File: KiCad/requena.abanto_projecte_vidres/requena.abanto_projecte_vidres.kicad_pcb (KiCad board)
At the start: 4 copper layers, 107.8 x 82.4 mm, 90 parts, among them J1 Conn_01x05, J3 DE9_Pins, J4 DE9_Pins, J5 Conn_01x02, P1 282837-2, P2 282837-2, SW1 SW_Push_SPDT, SW2 SW_Push, SW3 SW_Omron_B3FS, SW4 SW_Omron_B3FS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

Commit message: --
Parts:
- moved R1 9.97 mm to (120.8, 45.9), turned to -90 degrees
- moved R3 9.38 mm to (109.6, 45.6), turned to 90 degrees
- moved R2 8.79 mm to (106.7, 45.6)
- moved C6 6.51 mm to (114.2, 51.8), turned to 180 degrees
- moved U3 3.76 mm to (114.3, 45.2), turned to -90 degrees
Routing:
- net SCK: track 38.5 -> 4.40 mm
- net SHUNT: track 26.8 -> 0.00 mm
- net CAN_RX: track 40.3 -> 61.8 mm
- net AN0: track 55.9 -> 41.0 mm, vias 2 -> 1
- net GND: track 98.7 -> 85.1 mm, vias 94 -> 85
- net IRQ: track 37.4 -> 25.1 mm
- net REALIMENTACION_NOINV: track 12.2 -> 0.00 mm
- net OUTJUMPER: track 24.7 -> 13.4 mm
- net OUTSHUNT: track 9.67 -> 0.00 mm
- net OUTNOINV: track 8.93 -> 0.00 mm
- net VCC: track 50.3 -> 45.0 mm, vias 55 -> 52
- net SDA: track 43.1 -> 46.0 mm
- net CAN_TX: track 39.6 -> 37.3 mm
- net MCLR: track 17.2 -> 18.1 mm
- net MISO: track 35.0 -> 35.5 mm

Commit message: joan canals el mejor
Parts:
- C34, C35, C36, C37: moved to B.Cu
- moved FB1 96.7 mm to (86.9, 125.0)
- moved SW4 55.6 mm to (131.3, 106.0), turned to 90 degrees
- moved R8 47.9 mm to (131.9, 98.4), turned to 180 degrees
- moved J4 43.0 mm to (154.2, 100.5), turned to 0 degrees
- moved R9 38.3 mm to (131.7, 67.2), turned to 180 degrees
- moved SW3 34.6 mm to (140.6, 90.3), turned to 90 degrees
- moved J3 32.6 mm to (186.6, 100.5), turned to 0 degrees
- moved SW5 31.9 mm to (131.3, 74.7), turned to 90 degrees
- moved R7 31.6 mm to (141.2, 82.8), turned to 180 degrees
- moved R11 29.9 mm to (160.5, 96.8), turned to 180 degrees
- moved SW6 28.2 mm to (131.2, 90.3), turned to 90 degrees
- moved R10 27.5 mm to (131.7, 82.6), turned to 180 degrees
- moved SW2 24.1 mm to (140.5, 105.7), turned to -90 degrees
- moved U5 23.5 mm to (160.5, 91.3), turned to -90 degrees
- moved C34 21.8 mm to (194.4, 83.9)
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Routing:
- net CAN_RX: track 61.8 -> 6.03 mm, vias 2 -> 0
- net UP_W: track 67.3 -> 20.8 mm
- net DOWN_W: track 78.3 -> 36.8 mm, vias 0 -> 2
- net AN0: track 41.0 -> 1.53 mm
- net OUTJUMPER: track 13.4 -> 45.7 mm, vias 0 -> 2
- net SCK: track 4.40 -> 36.5 mm
- net CAN_TX: track 37.3 -> 6.11 mm
- net CLOSE_D: track 56.0 -> 32.5 mm
- net OPEN_D: track 44.9 -> 29.6 mm
- net PWM: track 31.3 -> 16.5 mm
- net UART_RX: track 54.3 -> 41.2 mm
- net IRQ: track 25.1 -> 37.4 mm
- net CLOSED_FC: track 12.0 -> 23.4 mm
- net INA: track 27.8 -> 39.0 mm
- net INB: track 34.0 -> 44.2 mm
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
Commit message: algunes millores
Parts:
- added TP1: TestPoint, TestPoint:TestPoint_Pad_1.5x1.5mm, F.Cu at (181.8, 86.1)
- added TP3: TestPoint, TestPoint:TestPoint_Pad_1.5x1.5mm, B.Cu at (193.6, 97.3)
- added TP4: TestPoint, TestPoint:TestPoint_Pad_1.5x1.5mm, B.Cu at (181.9, 99.9)
- added TP5: TestPoint, TestPoint:TestPoint_Pad_1.5x1.5mm, B.Cu at (136.0, 58.5)
- C20, C26: value C_Small -> 150 pF
- C27, C28: value C_Small -> 22 pF
- C29, C30: value C_Small -> 47 pF
- C31: value C_Small -> 1nF
- C32: value C_Small -> 100nF
- L1, L2: value L -> 2.2 uH
- L3: value L -> 1.5 uH
- R15, R16: value R -> 1.5
- R17: value R -> 2,2 k
- R18: value R -> 1k
- moved FB1 26.1 mm to (112.8, 121.9)
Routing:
- net AN0: track 1.53 -> 65.7 mm, vias 1 -> 2
- net PWM: track 16.5 -> 43.1 mm
- net VCC: track 53.8 -> 59.0 mm
- net UART_RX: track 41.2 -> 45.9 mm
- net UART_TX: track 44.6 -> 48.6 mm
- net GND: track 79.2 -> 82.1 mm

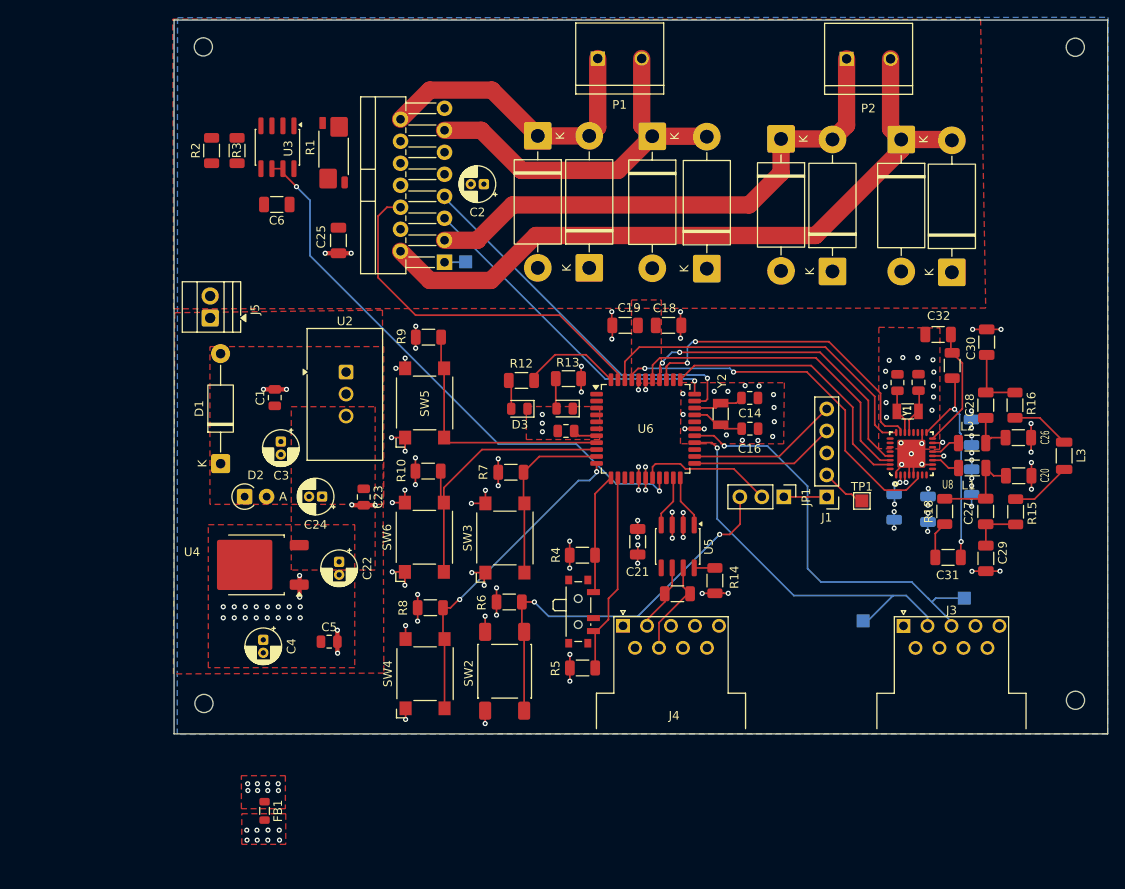
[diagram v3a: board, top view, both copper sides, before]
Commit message: faltan tests points
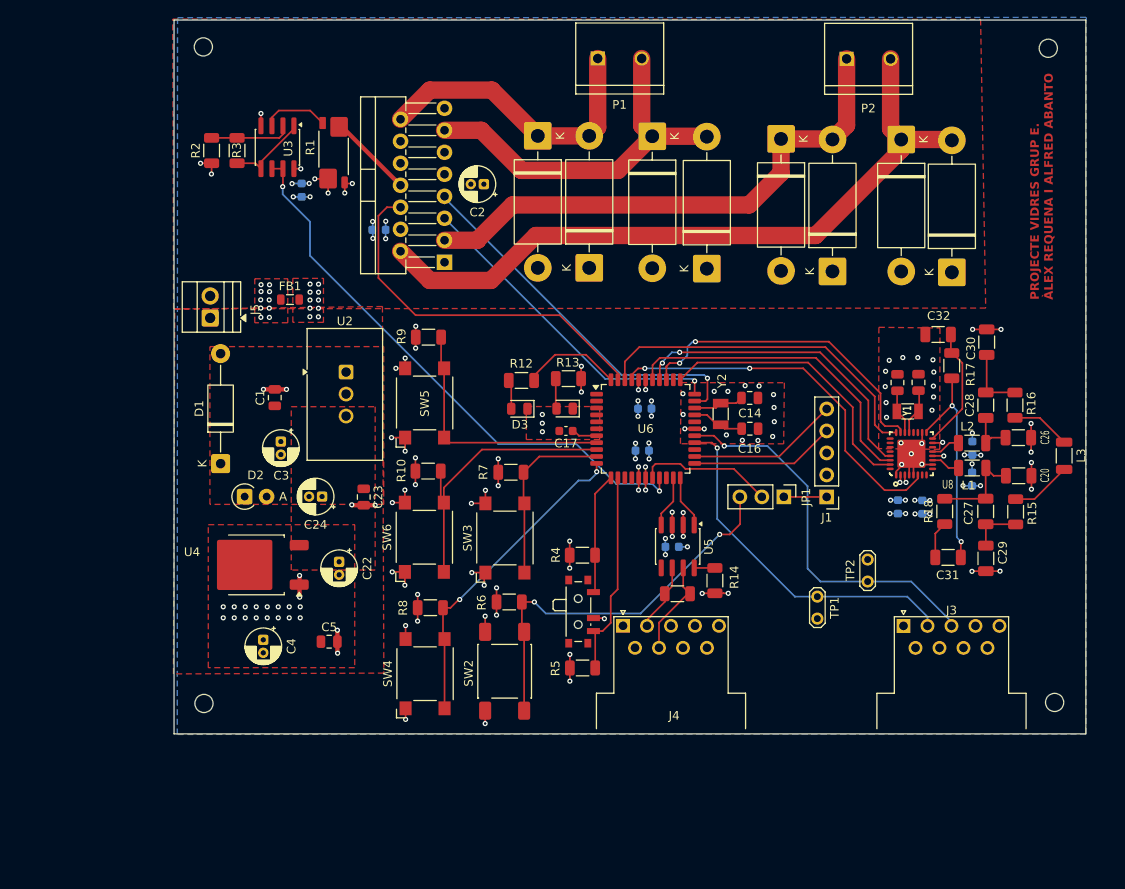
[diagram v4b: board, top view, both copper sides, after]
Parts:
- removed TP3, TP4, TP5: TestPoint, TestPoint:TestPoint_Pad_1.5x1.5mm
- added TP2: TestPoint_2Pole, TestPoint:TestPoint_2Pads_Pitch2.54mm_Drill0.8mm, F.Cu at (182.4, 95.4)
- C17: footprint Capacitor_SMD:C_0805_2012Metric -> Capacitor_SMD:C_0603_1608Metric
- C18, C19, C21, C25, C6: footprint Capacitor_SMD:C_1206_3216Metric -> Capacitor_SMD:C_0603_1608Metric; moved to B.Cu
- C34, C35, C36, C37: footprint Capacitor_SMD:C_1206_3216Metric -> Capacitor_SMD:C_0603_1608Metric
- R17: value 2,2 k -> 2.2k
- TP1: value TestPoint -> TestPoint_2Pole; footprint TestPoint:TestPoint_Pad_1.5x1.5mm -> TestPoint:TestPoint_2Pads_Pitch2.54mm_Drill0.8mm
- moved FB1 59.1 mm to (115.7, 62.8), turned to 0 degrees
- moved C18 14.8 mm to (156.4, 80.2)
- moved TP1 12.2 mm to (176.6, 97.1), turned to -90 degrees
- moved C19 9.88 mm to (156.7, 75.4), turned to 180 degrees
- moved C25 4.84 mm to (126.0, 54.8), turned to 180 degrees
- moved C21 4.02 mm to (159.9, 91.4), turned to 0 degrees
- moved C6 3.31 mm to (117.1, 50.2), turned to -90 degrees
- moved REF** 3.12 mm to (203.3, 33.8)
- moved REF** 2.42 mm to (204.0, 109.3)
- moved C35 1.84 mm to (194.5, 80.0)
- moved C36 0.71 mm to (188.8, 86.8)
- moved C37 0.44 mm to (185.9, 86.7)
- moved C34 0.35 mm to (194.5, 83.5)
- moved R17 0.05 mm to (192.2, 70.4), turned to 90 degrees
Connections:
- net Net-(C20-Pad1) renamed O
- net Net-(C26-Pad2) renamed I
- net Net-(C27-Pad2) renamed A
- net Net-(C28-Pad2) renamed E
- net Net-(C31-Pad2) renamed U
- net Net-(L3-Pad1) renamed L1
- net Net-(L3-Pad2) renamed L2
- net Net-(U8-TX1) renamed TX1
- net Net-(U8-TX2) renamed TX2
- C31 pad 1: Net-(U8-RX) -> RX
- C32 pad 1: Net-(U8-VMID) -> VMID
- R17 pad 1: Net-(U8-VMID) -> RX
- R17 pad 2: Net-(U8-RX) -> VMID
- TP1 pad 1: VCC -> UART_RX
- U8 pad 16: Net-(U8-VMID) -> VMID
- U8 pad 17: Net-(U8-RX) -> RX
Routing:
- net RX: track 0.00 -> 25.5 mm, vias 0 -> 2
- net Net-(U8-RX): track 24.9 -> 0.00 mm, vias 2 -> 0
- net VMID: track 0.00 -> 13.8 mm
- net Net-(U8-VMID): track 13.8 -> 0.00 mm
- net SHUNT: track 0.00 -> 9.89 mm
- net OUTNOINV: track 0.00 -> 9.55 mm
- net REALIMENTACION_NOINV: track 0.00 -> 9.39 mm
- net GND: track 82.1 -> 91.3 mm, vias 88 -> 102
- net OUTSHUNT: track 0.00 -> 7.75 mm
- net VCC: track 59.0 -> 51.8 mm, vias 57 -> 59
- net UART_RX: track 45.9 -> 41.2 mm
- net UART_TX: track 48.6 -> 44.6 mm
- net V_BAT: track 0.00 -> 2.08 mm, vias 0 -> 2
- net IRQ: track 37.4 -> 36.9 mm
- net GNDPWR: vias 12 -> 14
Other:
- board size 107.8 x 82.4 mm -> 105.3 x 82.4 mm
- board text added: "PROJECTE VIDRES GRUP E. ÀLEX REQUENA I ALFRED ABANTO"

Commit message: --
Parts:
- added TP3: TestPoint_2Pole, TestPoint:TestPoint_2Pads_Pitch2.54mm_Drill0.8mm, F.Cu at (176.5, 106.1)
- moved TP2 1.30 mm to (181.6, 94.4)
- moved TP1 0.95 mm to (176.7, 98.1)
- moved REF** 0.17 mm to (203.5, 33.8)

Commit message: alfred butanero
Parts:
- moved VCC 65.7 mm to (110.9, 109.8)
- moved UART_RX 0.99 mm to (177.1, 97.2), turned to -45 degrees
- moved UART_TX 0.92 mm to (181.7, 95.3), turned to 135 degrees
- moved D2 0.23 mm to (110.7, 85.6)
- renumbered TP1 to UART_RX, TP2 to UART_TX, TP3 to VCC
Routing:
- net IRQ: track 36.9 -> 39.1 mm
- net SDA: track 40.1 -> 42.3 mm
- net SCK: track 36.5 -> 38.1 mm
- net MOSI: track 37.0 -> 37.9 mm
- net MISO: track 32.4 -> 32.9 mm

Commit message: xd
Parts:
- added AN0: TestPoint_2Pole, TestPoint:TestPoint_2Pads_Pitch2.54mm_Drill0.8mm, F.Cu at (118.1, 55.8)
- added INA1: TestPoint_2Pole, TestPoint:TestPoint_2Pads_Pitch2.54mm_Drill0.8mm, F.Cu at (146.3, 66.2)
- added INB1: TestPoint_2Pole, TestPoint:TestPoint_2Pads_Pitch2.54mm_Drill0.8mm, F.Cu at (151.1, 67.3)
- added IRQ1: TestPoint_2Pole, TestPoint:TestPoint_2Pads_Pitch2.54mm_Drill0.8mm, F.Cu at (177.6, 65.2)
- added MISO-MOSI1: TestPoint_2Pole, TestPoint:TestPoint_2Pads_Pitch2.54mm_Drill0.8mm, F.Cu at (175.6, 69.9)
- added OUTSHUNT1: TestPoint_2Pole, TestPoint:TestPoint_2Pads_Pitch2.54mm_Drill0.8mm, F.Cu at (116.2, 40.1)
- added PWM1: TestPoint_2Pole, TestPoint:TestPoint_2Pads_Pitch2.54mm_Drill0.8mm, F.Cu at (138.5, 64.6)
- added SCK-SDA1: TestPoint_2Pole, TestPoint:TestPoint_2Pads_Pitch2.54mm_Drill0.8mm, F.Cu at (169.8, 67.6)
- added VBAT1: TestPoint_2Pole, TestPoint:TestPoint_2Pads_Pitch2.54mm_Drill0.8mm, F.Cu at (119.0, 109.4)
- added V_OUT_DCDC1: TestPoint_2Pole, TestPoint:TestPoint_2Pads_Pitch2.54mm_Drill0.8mm, F.Cu at (124.5, 109.4)
- moved VCC1 0.38 mm to (110.9, 109.4)
- renumbered UART_RX to UART_RX1, UART_TX to UART_TX1, VCC to VCC1
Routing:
- net OUTSHUNT: track 7.75 -> 8.49 mm

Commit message: huellas arregladas
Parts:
- C2, C3: value 470uF -> 47uF
- R1: value 50m -> 25m
- SW2: footprint Button_Switch_SMD:SW_Push_1P1T_NO_E-Switch_TL3301NxxxxxG -> Button_Switch_SMD:SW_SPST_Omron_B3FS-100xP
- Y1: value 27.12 MHz -> Crystal_GND24; footprint Crystal:Crystal_SMD_3215-2Pin_3.2x1.5mm -> Crystal:Crystal_SMD_3225-4Pin_3.2x2.5mm
- Y2: value 8 MHz -> Crystal_GND24; footprint Crystal:Crystal_SMD_3215-2Pin_3.2x1.5mm -> Crystal:Crystal_SMD_2520-4Pin_2.5x2.0mm
- moved Y2 21.5 mm to (186.9, 75.0), turned to -45 degrees
- moved Y1 20.7 mm to (166.4, 75.8), turned to 45 degrees
- moved V_OUT_DCDC1 15.9 mm to (124.7, 93.5), turned to -90 degrees
- moved C15 2.83 mm to (188.4, 71.1)
- moved C13 2.78 mm to (185.9, 71.0)
- moved VBAT1 2.23 mm to (121.2, 109.4)
- moved C16 2.07 mm to (170.8, 77.1)
- moved C14 1.93 mm to (170.7, 74.4)
- moved C22 0.89 mm to (120.5, 93.3)
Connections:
- C13 pad 1: OSC2RFID -> OSC1RFID
- C14 pad 1: OSC2 -> OSC1
- C15 pad 1: OSC1RFID -> OSC2RFID
- C16 pad 1: OSC1 -> OSC2
- U6 pad 30: OSC1 -> OSC2
- U6 pad 31: OSC2 -> OSC1
- Y1 pad 1: OSC2RFID -> OSC2
- Y1 pad 2: OSC1RFID -> GND
- Y2 pad 1: OSC2 -> OSC1RFID
- Y2 pad 2: OSC1 -> GND
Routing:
- net OSC2: track 5.92 -> 7.92 mm
- net OSC1: track 6.09 -> 7.84 mm
- net GND: track 91.3 -> 89.9 mm
- net OSC2RFID: track 5.90 -> 6.63 mm
- net OSC1RFID: track 5.92 -> 6.58 mm
